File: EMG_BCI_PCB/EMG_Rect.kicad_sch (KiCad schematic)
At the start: 24 parts, among them J2 2.54 mm header, U3 ADA4807-4ARUZ, U8 MCP1501-18xCH

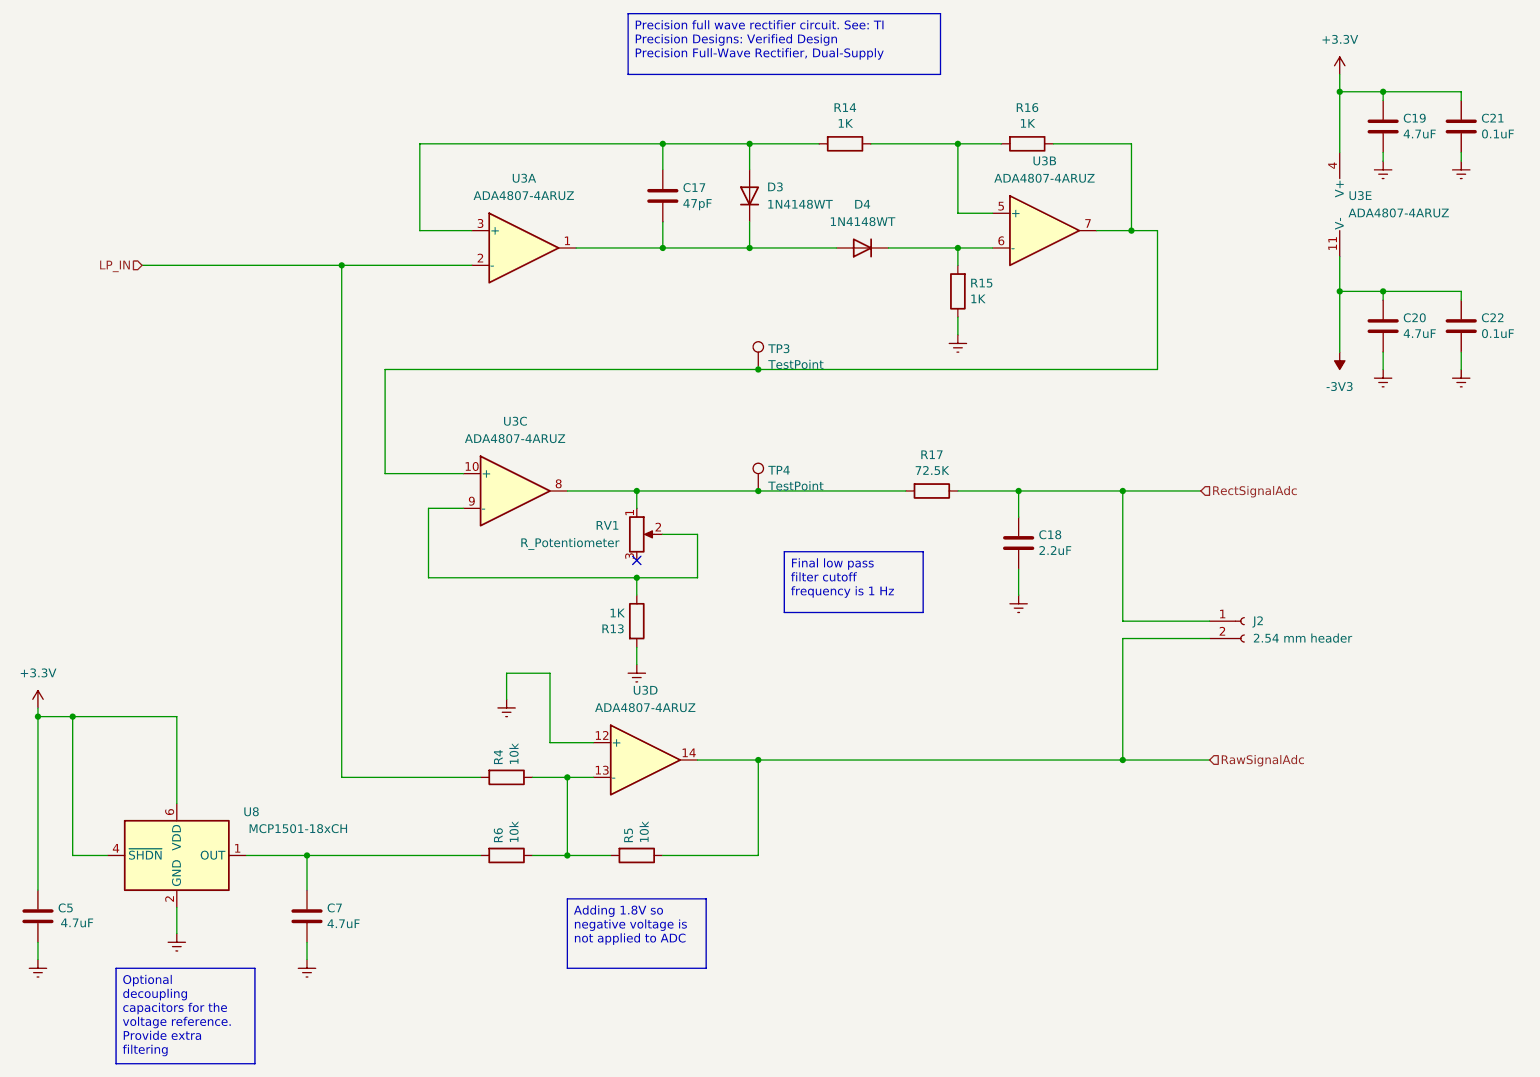
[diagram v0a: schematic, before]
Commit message: Ordering the components
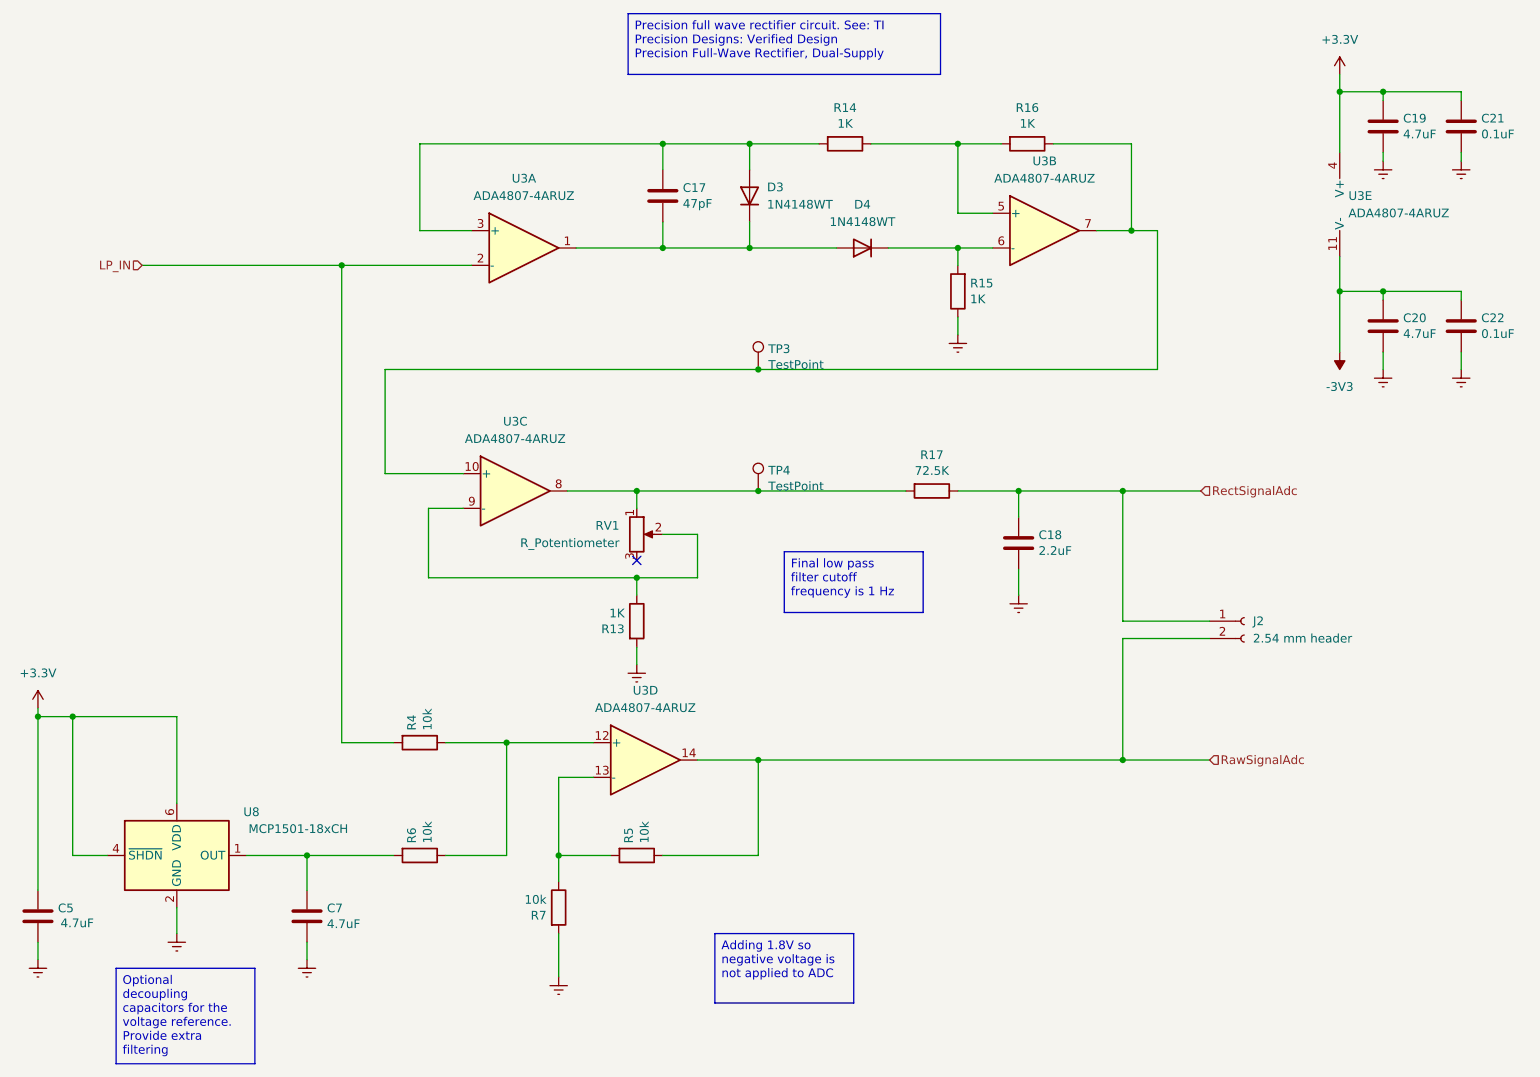
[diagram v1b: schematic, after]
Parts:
- added R7: 10k, Resistor_SMD:R_0603_1608Metric_Pad0.98x0.95mm_HandSolder, symbol Device:R
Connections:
- net Earth: now also R7.2; no longer U3.12 (+)
- net at R4.1, R6.1: now also U3.12 (+); no longer R5.2, U3.13 (-)
- new net: R5.2, R7.1, U3.13 (-)
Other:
- moved on the sheet: R4, R6
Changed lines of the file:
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@@
 	(text_box "Adding 1.8V so negative voltage is not applied to ADC"
 		(exclude_from_sim no)
-		(at 102.87 147.32 0)
+		(at 124.46 152.4 0)
 		(size 20.32 10.16)
 		(margins 0.9525 0.9525 0.9525 0.9525)
@@
 	)
 	(junction
+		(at 93.98 124.46)
+		(diameter 0)
+		(color 0 0 0 0)
+	)
+	(junction
 		(at 130.81 127)
 		(diameter 0)
@@
 	)
 	(junction
+		(at 101.6 140.97)
+		(diameter 0)
+		(color 0 0 0 0)
+	)
+	(junction
 		(at 184.15 87.63)
 		(diameter 0)
@@
 	)
 	(junction
-		(at 102.87 129.54)
-		(diameter 0)
-		(color 0 0 0 0)
-	)
-	(junction
 		(at 222.25 29.21)
 		(diameter 0)
@@
 	)
 	(junction
-		(at 102.87 140.97)
-		(diameter 0)
-		(color 0 0 0 0)
-	)
-	(junction
 		(at 184.15 127)
 		(diameter 0)
@@
 	(wire
 		(pts
-			(xy 215.9 53.34) (xy 215.9 58.42)
+			(xy 85.09 140.97) (xy 93.98 140.97)
 		)
 		(stroke
@@
 	(wire
 		(pts
-			(xy 184.15 127) (xy 196.85 127)
+			(xy 215.9 53.34) (xy 215.9 58.42)
 		)
 		(stroke
@@
 	(wire
 		(pts
-			(xy 113.03 87.63) (xy 130.81 87.63)
+			(xy 184.15 127) (xy 196.85 127)
 		)
 		(stroke
@@
 	(wire
 		(pts
-			(xy 130.81 69.85) (xy 76.2 69.85)
+			(xy 93.98 124.46) (xy 106.68 124.46)
 		)
 		(stroke
@@
 	(wire
 		(pts
-			(xy 129.54 36.83) (xy 116.84 36.83)
+			(xy 113.03 87.63) (xy 130.81 87.63)
 		)
 		(stroke
@@
 	(wire
 		(pts
-			(xy 102.87 129.54) (xy 106.68 129.54)
+			(xy 130.81 69.85) (xy 76.2 69.85)
 		)
 		(stroke
@@
 	(wire
 		(pts
-			(xy 215.9 58.42) (xy 215.9 67.31)
+			(xy 129.54 36.83) (xy 116.84 36.83)
 		)
 		(stroke
@@
 	(wire
 		(pts
-			(xy 222.25 30.48) (xy 222.25 29.21)
+			(xy 215.9 58.42) (xy 215.9 67.31)
 		)
 		(stroke
@@
 	(wire
 		(pts
-			(xy 233.68 59.69) (xy 233.68 58.42)
+			(xy 222.25 30.48) (xy 222.25 29.21)
 		)
 		(stroke
@@
 	(wire
 		(pts
-			(xy 168.91 87.63) (xy 160.02 87.63)
+			(xy 233.68 59.69) (xy 233.68 58.42)
 		)
 		(stroke
@@
 	(wire
 		(pts
-			(xy 100.33 124.46) (xy 100.33 114.3)
+			(xy 101.6 140.97) (xy 101.6 144.78)
 		)
 		(stroke
@@
 	(wire
 		(pts
-			(xy 100.33 114.3) (xy 93.98 114.3)
+			(xy 168.91 87.63) (xy 160.02 87.63)
 		)
 		(stroke
@@
 	(wire
 		(pts
-			(xy 69.85 129.54) (xy 69.85 54.61)
+			(xy 69.85 124.46) (xy 69.85 54.61)
 		)
 		(stroke
@@
 	(wire
 		(pts
+			(xy 106.68 129.54) (xy 101.6 129.54)
+		)
+		(stroke
+			(width 0)
+			(type default)
+		)
+	)
+	(wire
+		(pts
 			(xy 64.77 140.97) (xy 64.77 146.05)
 		)
@@
 	(wire
 		(pts
-			(xy 69.85 54.61) (xy 88.9 54.61)
+			(xy 101.6 129.54) (xy 101.6 140.97)
 		)
 		(stroke
@@
 	(wire
 		(pts
-			(xy 25.4 153.67) (xy 25.4 156.21)
+			(xy 69.85 54.61) (xy 88.9 54.61)
 		)
 		(stroke
@@
 	(wire
 		(pts
-			(xy 130.81 140.97) (xy 130.81 127)
+			(xy 25.4 153.67) (xy 25.4 156.21)
 		)
 		(stroke
@@
 	(wire
 		(pts
-			(xy 90.17 129.54) (xy 69.85 129.54)
+			(xy 130.81 140.97) (xy 130.81 127)
 		)
 		(stroke
@@
 	(wire
 		(pts
-			(xy 109.22 140.97) (xy 102.87 140.97)
+			(xy 77.47 124.46) (xy 69.85 124.46)
 		)
 		(stroke
@@
 	(wire
 		(pts
-			(xy 97.79 140.97) (xy 102.87 140.97)
-		)
-		(stroke
-			(width 0)
-			(type default)
-		)
-	)
-	(wire
-		(pts
 			(xy 185.42 49.53) (xy 185.42 36.83)
 		)
@@
 	(wire
 		(pts
-			(xy 104.14 52.07) (xy 116.84 52.07)
+			(xy 93.98 140.97) (xy 93.98 124.46)
 		)
 		(stroke
@@
 	(wire
 		(pts
-			(xy 106.68 124.46) (xy 100.33 124.46)
+			(xy 104.14 52.07) (xy 116.84 52.07)
 		)
 		(stroke
@@
 	(wire
 		(pts
+			(xy 101.6 140.97) (xy 109.22 140.97)
+		)
+		(stroke
+			(width 0)
+			(type default)
+		)
+	)
+	(wire
+		(pts
 			(xy 113.03 113.03) (xy 113.03 110.49)
 		)
@@
 	(wire
 		(pts
-			(xy 81.28 49.53) (xy 88.9 49.53)
+			(xy 85.09 124.46) (xy 93.98 124.46)
 		)
 		(stroke
@@
 	(wire
 		(pts
-			(xy 160.02 36.83) (xy 147.32 36.83)
+			(xy 81.28 49.53) (xy 88.9 49.53)
 		)
 		(stroke
@@
 	(wire
 		(pts
-			(xy 160.02 46.99) (xy 160.02 36.83)
+			(xy 160.02 36.83) (xy 147.32 36.83)
 		)
 		(stroke
@@
 	(wire
 		(pts
-			(xy 97.79 129.54) (xy 102.87 129.54)
+			(xy 160.02 46.99) (xy 160.02 36.83)
 		)
 		(stroke
@@
 	(wire
 		(pts
-			(xy 93.98 114.3) (xy 93.98 118.11)
+			(xy 101.6 152.4) (xy 101.6 158.75)
 		)
 		(stroke
@@
 	(wire
 		(pts
-			(xy 64.77 140.97) (xy 90.17 140.97)
-		)
-		(stroke
-			(width 0)
-			(type default)
-		)
-	)
-	(wire
-		(pts
-			(xy 102.87 140.97) (xy 102.87 129.54)
+			(xy 64.77 140.97) (xy 77.47 140.97)
 		)
 		(stroke
@@
 	(symbol
 		(lib_id "power:Earth")
-		(at 93.98 118.11 0)
+		(at 101.6 158.75 0)
 		(unit 1)
 		(exclude_from_sim no)
@@
 		(dnp no)
 		(property "Reference" "#PWR02"
-			(at 93.98 124.46 0)
+			(at 101.6 165.1 0)
 			(effects
 				(font
@@
 		)
 		(property "Value" "Earth"
-			(at 93.98 121.92 0)
+			(at 101.6 162.56 0)
 			(effects
 				(font
@@
 		)
 		(property "Footprint" ""
-			(at 93.98 118.11 0)
+			(at 101.6 158.75 0)
 			(effects
 				(font
@@
 		)
 		(property "Datasheet" "~"
-			(at 93.98 118.11 0)
+			(at 101.6 158.75 0)
 			(effects
 				(font
@@
 		)
 		(property "Description" ""
-			(at 93.98 118.11 0)
+			(at 101.6 158.75 0)
 			(effects
 				(font
@@
 	(symbol
 		(lib_id "Device:R")
-		(at 93.98 129.54 270)
+		(at 81.28 124.46 270)
 		(unit 1)
 		(exclude_from_sim no)
@@
 		(dnp no)
 		(property "Reference" "R4"
-			(at 92.8116 127.762 0)
+			(at 80.1116 122.682 0)
 			(effects
 				(font
@@
 		)
 		(property "Value" "10k"
-			(at 95.123 127.762 0)
+			(at 82.423 122.682 0)
 			(effects
 				(font
@@
 		)
 		(property "Footprint" "Resistor_SMD:R_0603_1608Metric_Pad0.98x0.95mm_HandSolder"
-			(at 93.98 127.762 90)
+			(at 81.28 122.682 90)
 			(effects
 				(font
@@
 		)
 		(property "Datasheet" "~"
-			(at 93.98 129.54 0)
+			(at 81.28 124.46 0)
 			(effects
 				(font
@@
 		)
 		(property "Description" ""
-			(at 93.98 129.54 0)
+			(at 81.28 124.46 0)
 			(effects
 				(font
@@
 	)
 	(symbol
+		(lib_id "Device:R")
+		(at 101.6 148.59 0)
+		(unit 1)
+		(exclude_from_sim no)
+		(in_bom yes)
+		(on_board yes)
+		(dnp no)
+		(property "Reference" "R7"
+			(at 99.822 149.7584 0)
+			(effects
+				(font
+					(size 1.27 1.27)
+				)
+				(justify right)
+			)
+		)
+		(property "Value" "10k"
+			(at 99.822 147.447 0)
+			(effects
+				(font
+					(size 1.27 1.27)
+				)
+				(justify right)
+			)
+		)
+		(property "Footprint" "Resistor_SMD:R_0603_1608Metric_Pad0.98x0.95mm_HandSolder"
+			(at 99.822 148.59 90)
+			(effects
+				(font
+					(size 1.27 1.27)
+				)
+				(hide yes)
+			)
+		)
+		(property "Datasheet" "~"
+			(at 101.6 148.59 0)
+			(effects
+				(font
+					(size 1.27 1.27)
+				)
+				(hide yes)
+			)
+		)
+		(property "Description" ""
+			(at 101.6 148.59 0)
+			(effects
+				(font
+					(size 1.27 1.27)
+				)
+			)
+		)
+		(pin "1"
+		)
+		(pin "2"
+		)
+		(instances
+			(project "EMG_BCI_PCB"
+				(path "/55cf2478-b5ba-45ce-afa6-3f75a1bb5fb4/00000000-0000-0000-0000-00005f16ee03"
+					(reference "R7")
+					(unit 1)
+				)
+			)
+		)
+	)
+	(symbol
 		(lib_id "power:Earth")
 		(at 25.4 156.21 0)
@@
 	(symbol
 		(lib_id "Device:R")
-		(at 93.98 140.97 270)
+		(at 81.28 140.97 270)
 		(unit 1)
 		(exclude_from_sim no)
@@
 		(dnp no)
 		(property "Reference" "R6"
-			(at 92.8116 139.192 0)
+			(at 80.1116 139.192 0)
 			(effects
 				(font
@@
 		)
 		(property "Value" "10k"
-			(at 95.123 139.192 0)
+			(at 82.423 139.192 0)
 			(effects
 				(font
@@
 		)
 		(property "Footprint" "Resistor_SMD:R_0603_1608Metric_Pad0.98x0.95mm_HandSolder"
-			(at 93.98 139.192 90)
+			(at 81.28 139.192 90)
 			(effects
 				(font
@@
 		)
 		(property "Datasheet" "~"
-			(at 93.98 140.97 0)
+			(at 81.28 140.97 0)
 			(effects
 				(font
@@
 		)
 		(property "Description" ""
-			(at 93.98 140.97 0)
+			(at 81.28 140.97 0)
 			(effects
 				(font

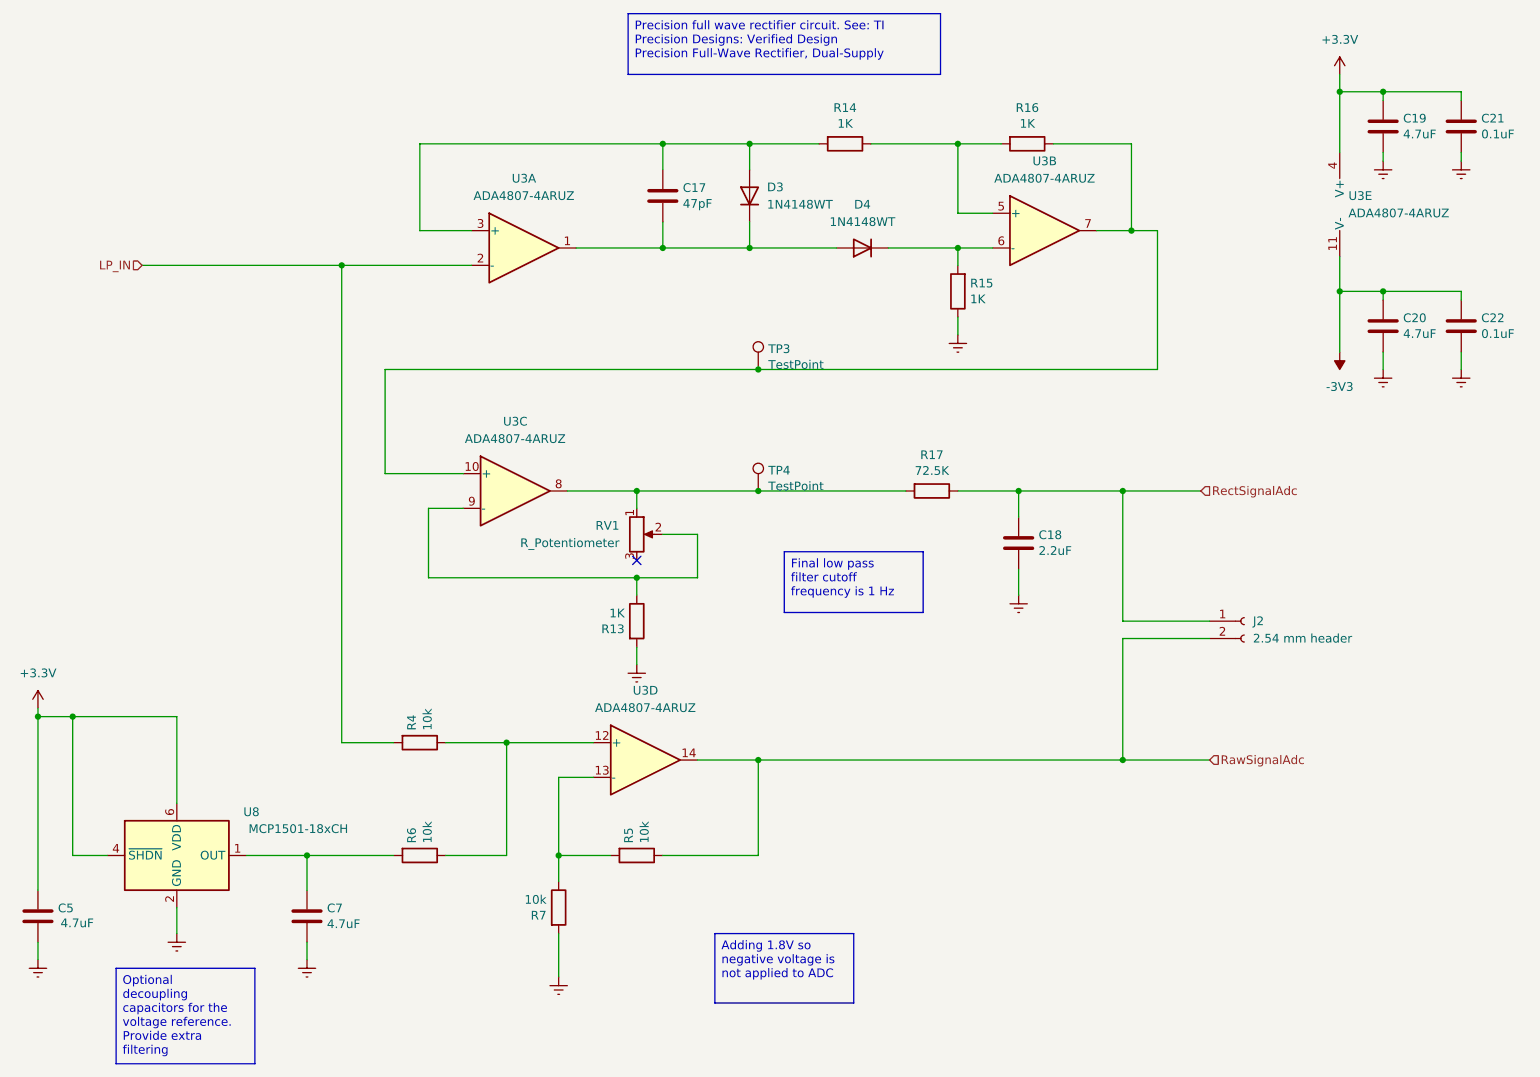
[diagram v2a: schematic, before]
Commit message: corrected the active rectifier schematic
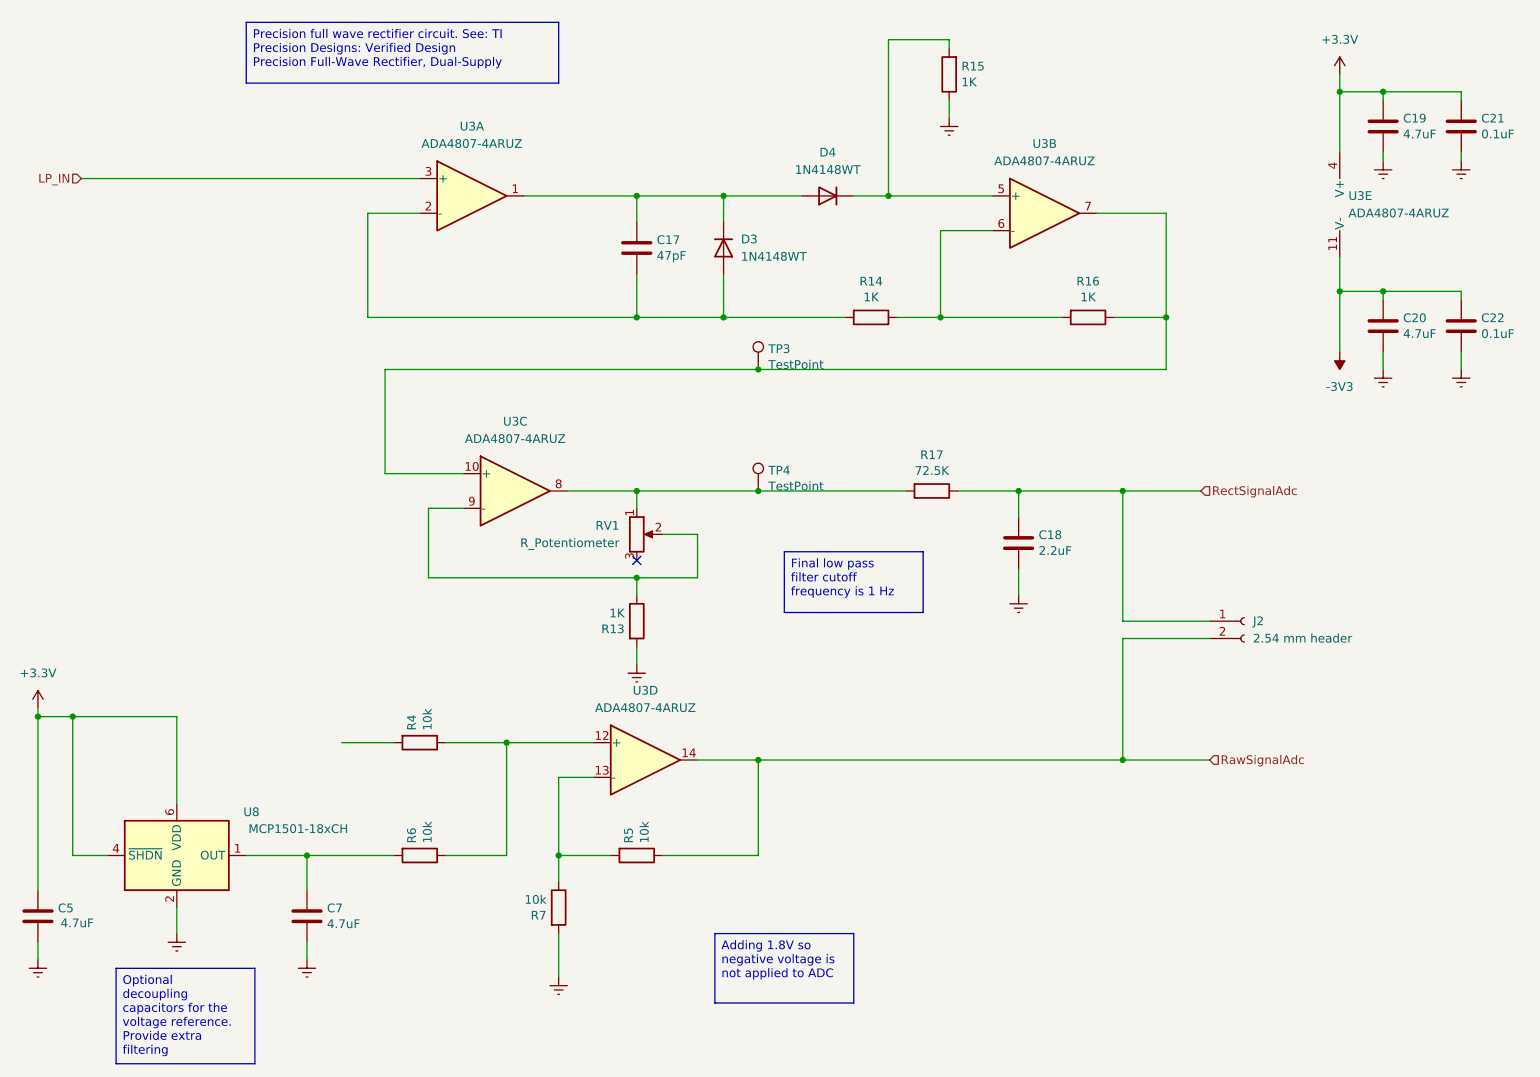
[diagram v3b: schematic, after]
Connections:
- net LP_IN: now also U3.3 (+); no longer R4.2, U3.2 (-)
- net at D3.2 (A), R14.2: now also C17.2, U3.2 (-); no longer C17.1, U3.3 (+)
- net at D3.1 (K), D4.2 (A), U3.1: now also C17.1; no longer C17.2
- net at R14.1, R16.2: now also U3.6 (-); no longer U3.5 (+)
- net at D4.1 (K), R15.2: now also U3.5 (+); no longer U3.6 (-)
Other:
- moved on the sheet: C17, D3, D4, R14, R15, R16, U3A, U3B
